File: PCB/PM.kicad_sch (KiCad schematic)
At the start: 4 parts, among them J4 TC0203620000G, J5 TC0203620000G, J6 TC0203620000G, J7 TC0203620000G

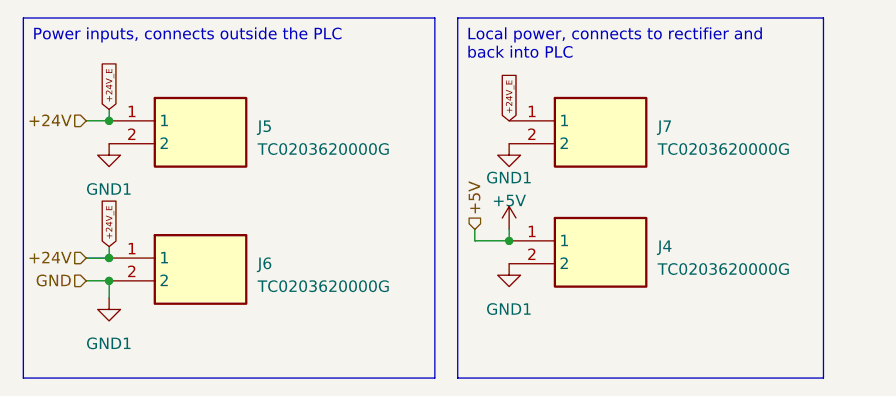
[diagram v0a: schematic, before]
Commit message: Redesigned, to utilize the ESP32 as the basis
* Implemented EEPROM
* Implemented RTC
* Implemented RS232 and 485
* Implemented CANBus
* Implemented everything
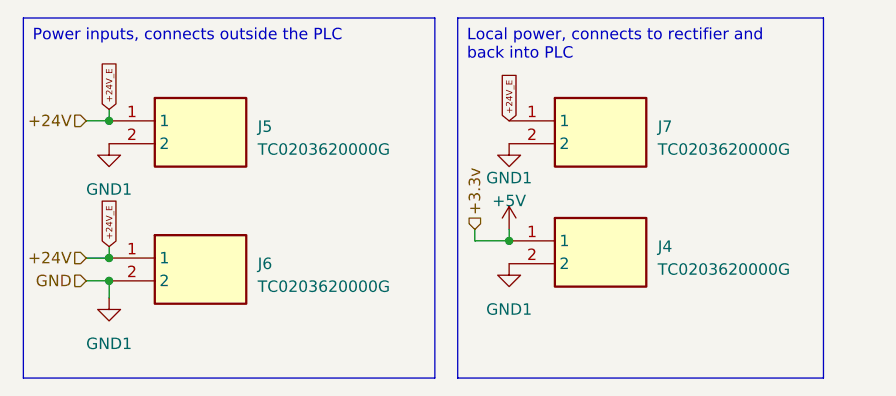
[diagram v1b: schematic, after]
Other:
- company: (none) -> UPB - FIIR - Roboți și sisteme de producție
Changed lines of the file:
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@@
 (kicad_sch (version 20230121) (generator eeschema)
   (paper "A4")
+  (title_block
+    (date "2023-04-23")
+    (rev "1")
+    (company "UPB - FIIR - Roboți și sisteme de producție")
+    (comment 1 "Alexandru-Ioan Anastasiu")
+  )
   (junction (at 123.19 116.84) (diameter 0) (color 0 0 0 0)
   )
@@
     (effects (font (size 1.27 1.27)) (justify right))
   )
-  (hierarchical_label "+5V" (shape input) (at 163.83 113.665 90) (fields_autoplaced)
+  (hierarchical_label "+3.3v" (shape input) (at 163.83 113.665 90) (fields_autoplaced)
     (effects (font (size 1.27 1.27)) (justify left))
   )
